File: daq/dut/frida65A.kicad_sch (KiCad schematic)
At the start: 99 parts, among them J1 SMA Molex 733910070, J10 DIFF/SE CFG, J11 SPI TP, J12 TP CLOCKS, J13 VIN CFG, J14 ATTEN CFG, J15 TP AMP, J2 SMA Molex 733910070, J3 SMA Molex 733910070, J4 RJ45 Molex 446200002, J5 DisplayPort Molex 472720024, J6 MiniFitJr Molex 469990014, J7 POWER, Q1 Q_PMOS_DGS, U1 ASIC FRIDA 65A, U2 TI LevelShifter SN74AXC8T245R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, U3 DiffAmp TI THS4541

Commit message: Renumber passives
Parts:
- JP1: renamed from JP2; now in the parts list
- JP2: renamed from JP3; now in the parts list
- Q1: footprint (none) -> Package_TO_SOT_SMD:SOT-23-3
- R27: renamed from R26; footprint (none) -> Resistor_SMD:R_0402_1005Metric
- R28: renamed from R27; footprint (none) -> Resistor_SMD:R_0402_1005Metric
- R29: renamed from R28; footprint (none) -> Resistor_SMD:R_0402_1005Metric
- R30: renamed from R29; footprint (none) -> Resistor_SMD:R_0402_1005Metric
- renumbered C17 to C1, C2 to C10, C6 to C11, C23 to C12, C3 to C13, C7 to C14, C24 to C15, C4 to C16, C8 to C17, C25 to C18, C13 to C19, C32 to C2, C9 to C20, C18 to C21, C14 to C22, C10 to C23, C19 to C24, C15 to C25, C11 to C26, C20 to C27, C16 to C28, C12 to C29, C31 to C3, C21 to C30, C26 to C31, C27 to C32, C29 to C33, C28 to C34, C34 to C4, C33 to C5, C30 to C6, C1 to C7, C5 to C8, C22 to C9, FB3 to FB2, FB2 to FB3, H3 to H2, H2 to H3, J5 to J1, J6 to J10, J7 to J11, J4 to J12, J11 to J13, J12 to J2, J2 to J3, J1 to J4, J10 to J5, J14 to J6, J3 to J7, J15 to J8, J13 to J9, R13 to R1, R1 to R10, R3 to R11, R2 to R12, R4 to R13, R17 to R14, R14 to R15, R15 to R16, R36 to R17, R19 to R18, R18 to R19, R5 to R2, R35 to R20, R20 to R21, R21 to R22, R22 to R23, R23 to R24, R24 to R25, R25 to R26, R6 to R3, R30 to R31, R16 to R32, R34 to R33, R33 to R34, R32 to R35, R31 to R36, R7 to R4, R8 to R5, R9 to R6, R10 to R7, R11 to R8, R12 to R9, U3 to U1, U1 to U3
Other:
- moved on the sheet: C10, C11, C12, C13, C14, C15, C16, C17, C18, C19, C2, C20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

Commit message: Add new layout generator files and update board and docs files
Add new flow/layout files for parameter classes, tech layer mapping, raw export, MOSFET generator, and MOMCAP generator, and remove old layout files that are no longer used. Update IHP130 layout metadata and inline test setup, update pytest discovery for inline layout tests, update the three PDK submodule pointers to their new commits, update DAQ KiCad project files, and remove old docs files and env.sh.
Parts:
- added J6, J9: TERM CFG, Connector_PinHeader_2.54mm:PinHeader_2x04_P2.54mm_Vertical, symbol Connector_Generic:Conn_02x04_Odd_Even
- renumbered J9 to J10, J8 to J11, J10 to J12, J11 to J13, J12 to J14, J13 to J15, J6 to J7, J7 to J8, R17 to R15, R18 to R16, R19 to R17, R20 to R18, R15 to R19, R16 to R20, R23 to R21, R24 to R22, R21 to R23, R22 to R24
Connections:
- net CLK_COMP_N: now also J2.9 (Pin_9); no longer J2.10 (Pin_10)
- net CLK_COMP_P: now also J2.10 (Pin_10); no longer J2.9 (Pin_9)
- net CLK_LOGIC_N: now also J2.7 (Pin_7); no longer J2.8 (Pin_8)
- net CLK_LOGIC_P: now also J2.8 (Pin_8); no longer J2.7 (Pin_7)
- net COMP_OUT_N: now also J2.5 (Pin_5); no longer J2.6 (Pin_6)
- net COMP_OUT_P: now also J2.6 (Pin_6); no longer J2.5 (Pin_5)
- net GND: now also R35.2, J6.1 (Pin_1), J6.7 (Pin_7), J9.1 (Pin_1), J9.7 (Pin_7)
- net VDD_BDAQ: no longer R35.1
- net VIN_P_EXT: now also J6.3 (Pin_3); no longer R19.2
- net VOCM_EXT: now also J9.3 (Pin_3), J9.5 (Pin_5); no longer R23.1, R24.2
- net at J5.2 (Pin_2), J5.4 (Pin_4), R17.2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: now also J6.5 (Pin_5); no longer R20.2
- net at U2.21 (OE_N): now also R35.1; no longer R35.2
- new net: J6.2 (Pin_2), J6.4 (Pin_4), R20.2
- new net: J6.6 (Pin_6), J6.8 (Pin_8), R19.2
- new net: J9.6 (Pin_6), J9.8 (Pin_8), R24.2
- new net: J9.2 (Pin_2), J9.4 (Pin_4), R23.1
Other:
- note added: "50Ω:"
- note added: "DIR1 pull-up -> A1-A4 input DIR2 pull-up -> A5-A8 output"
- note added: "Disable R-divider when measuring VDD_DAC current"
- note added: "Disabled:"
- note added: "Enabled:"
- note added: "Open:"
- note removed: "DNP R-divider when measuring VDD_DAC current"
- moved on the sheet: C10, C11, C12, C13, C14, C15, C16, C17, C18, C19, C2, C20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

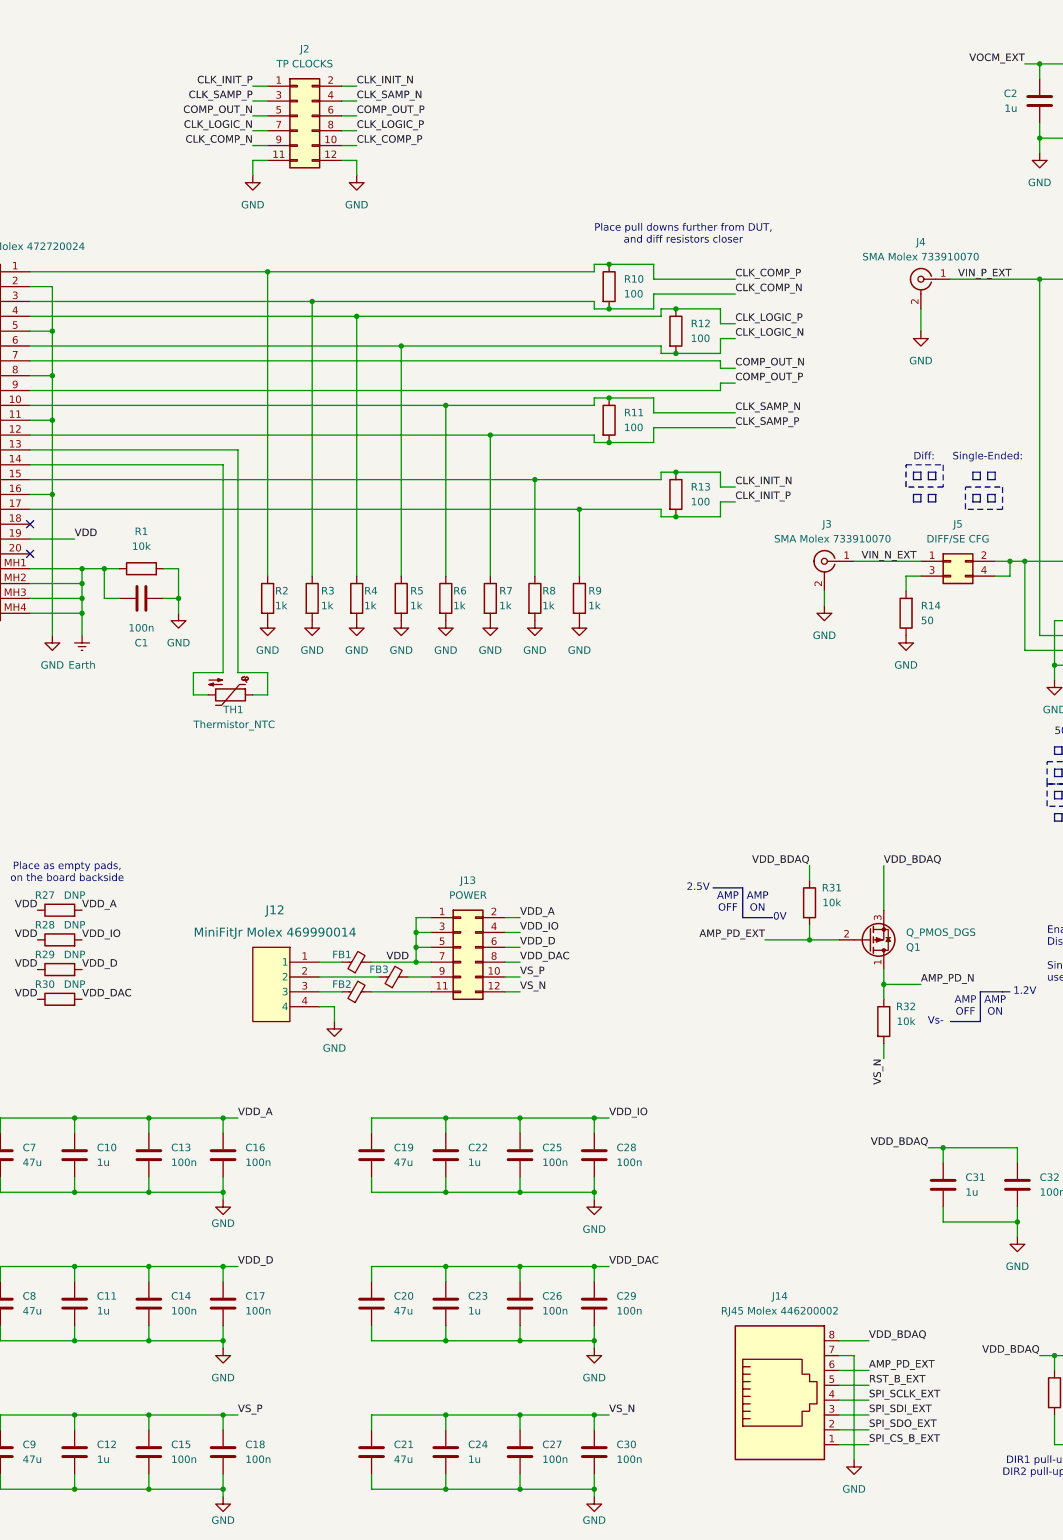
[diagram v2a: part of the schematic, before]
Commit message: Add support for image generation and outdir control
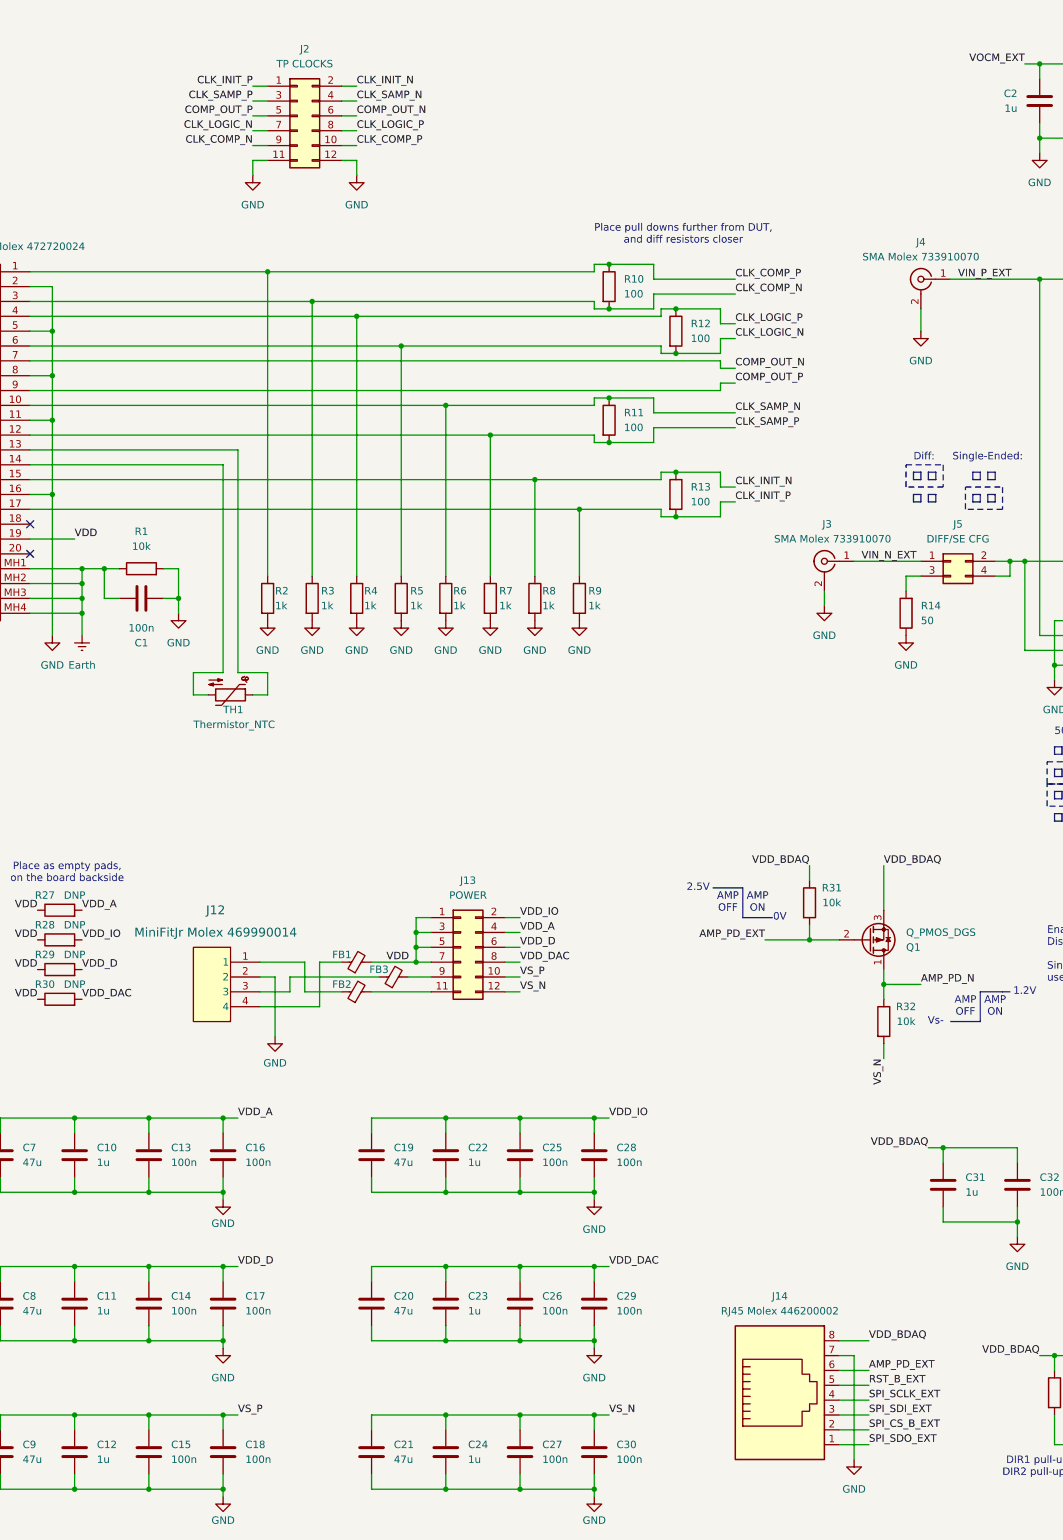
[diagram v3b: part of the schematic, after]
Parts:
- R27, R28, R29, R30: footprint Resistor_SMD:R_0402_1005Metric -> Resistor_SMD:R_0201_0603Metric
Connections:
- net COMP_OUT_N: now also J2.6 (Pin_6); no longer J2.5 (Pin_5)
- net COMP_OUT_P: now also J2.5 (Pin_5); no longer J2.6 (Pin_6)
- net GND: now also J12.2; no longer J12.4
- net SPI_CS_B_EXT: now also J14.2; no longer J14.1
- net SPI_SDO_EXT: now also J14.1; no longer J14.2
- net VDD_A: now also J13.4 (Pin_4); no longer J13.2 (Pin_2)
- net VDD_IO: now also J13.2 (Pin_2); no longer J13.4 (Pin_4)
- net at FB1.1: now also J12.4; no longer J12.1
- net at FB2.1: now also J12.1; no longer J12.3
- net at FB3.1: now also J12.3; no longer J12.2
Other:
- moved on the sheet: J12

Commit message: Finish pcb layout
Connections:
- net GND: now also J6.2 (Pin_2), J6.8 (Pin_8); no longer J6.1 (Pin_1), J6.7 (Pin_7)
- net VIN_P_EXT: now also J6.4 (Pin_4); no longer J6.3 (Pin_3)
- net at J5.2 (Pin_2), J5.4 (Pin_4), R17.2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: now also J6.6 (Pin_6); no longer J6.5 (Pin_5)
- new net: J6.1 (Pin_1), J6.3 (Pin_3), R20.2
- new net: J6.5 (Pin_5), J6.7 (Pin_7), R19.2
